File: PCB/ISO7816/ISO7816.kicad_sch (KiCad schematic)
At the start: 48 parts, among them J1 Conn_01x02, J3 Conn_01x08, J4 Conn_01x08, J6 USB-C-Socket-H, J7 TC2030-USB-NL-DS, Q1 BSS138PS, Q2 BSS138PS, Q3 BSS138PS, U1 ESP32-S3-MINI-1-N4R2, U2 TPS562246, U4 TPS22916CNYFPR, U5 TPS22916CNYFPR

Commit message: Schematic
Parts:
- removed C1, C9: C, RevK:C_0805, symbol Device:C
- removed C10, C11, C12, C13, C14, C7, C8: C, RevK:C_0201, symbol Device:C
- removed C2, C3, C4: C, RevK:C_0402, symbol Device:C
- removed C5: C, RevK:C_0603, symbol Device:C
- removed D4: ~, RevK:DFN1006-2L, symbol RevK:ES05D1MC10
- removed L1: L, RevK:L_5x5, symbol Device:L
- removed unit 1 of Q2
- removed R7: R, RevK:R_0201, symbol Device:R
- removed U2: TPS562246, RevK:SOT-563, symbol RevK:TPS562246
- added C15: 22uF 25V, RevK:C_0805, symbol Device:C
- added C16, C17: 100nF 25V, RevK:C_0402, symbol Device:C
- added C18, C21, C22, C23, C24, C25: 100nF, RevK:C_0201, symbol Device:C
- added C19: 18pF, RevK:C_0201, symbol Device:C
- added C20: 47uF 6V, RevK:C_0805, symbol Device:C
- added L2: 4.7uH, RevK:L_5x5, symbol Device:L
- added Q3: BSS138PS, RevK:SOT-363_SC-70-6, symbol RevK:BSS138PS
- added Q4: BSS84, Package_TO_SOT_SMD:SOT-23, symbol Transistor_FET:BSS84
- added R14, R15: 150k 1%, RevK:R_0201, symbol Device:R
- added R16: 33k 1%, RevK:R_0201, symbol Device:R
- added R17, R18, R19: 10k, RevK:R_0201, symbol Device:R
- added R20: 10R, RevK:R_0201, symbol Device:R
- added U2, U6: SN74LVC1T45DCK, Package_TO_SOT_SMD:SOT-363_SC-70-6, symbol Logic_LevelTranslator:SN74LVC1T45DCK
- added U3: TPS562246, RevK:SOT-563, symbol RevK:TPS562246
- C6: value C -> 1uF; footprint RevK:C_0402 -> RevK:C_0201
- J3, J4: now left out of the parts list
- R1: value R -> 20k; MPN C310173 -> (none)
- R2: value R -> 10k; footprint RevK:R_0402 -> RevK:R_0201
- R3: value R -> 10k; MPN C310173 -> (none)
- R4: value R -> 10k; MPN C320835 -> (none)
- renumbered Q3 to Q2
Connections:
- net +3.3V: now also C19.2, C20.1, C21.2, C22.2, C23.2, C24.2, C25.2, L2.2, R15.1, U2.1 (VCCA), U6.1 (VCCA); no longer R3.1
- net BST: now also C18.1, U3.4 (VBST)
- net C_3V3: now also U1.41 (GPIO45)
- net C_5V: now also U1.38 (GPIO42)
- net C_INSERT: now also U1.22 (GPIO18)
- net C_I/O: now also R1.2, Q3.3 (SP)
- net C_I/O_I: now also U1.28 (GPIO33)
- net C_RST: now also R20.2
- net C_VCC: now also R3.2, Q4.2 (S), U2.6 (VCCB), U6.6 (VCCB)
- net C_VCC_I: now also U1.36 (GPIO40)
- net C_VPP_I: now also U1.37 (GPIO41)
- net EN: now also R14.1, U3.5 (EN); no longer R1.1
- net FB: now also C19.1, R15.2, R16.1, U3.6 (VFB); no longer R3.2, R4.1
- net GND: now also R4.1, C15.2, C16.2, C17.2, C20.2, C21.1, C22.1, C23.1, C24.1, C25.1, Q3.1 (SN), Q3.4 (DP), R16.2, R17.2, R18.1, R19.1, U2.2 (GND), U3.3 (GND), U6.2 (GND); no longer Q2.4 (DP), R4.2
- net LED: now also U1.5 (GPIO1); no longer U1.27 (GPIO47)
- net SW: now also C18.2, L2.1, U3.2 (SW)
- net VBUS: now also C15.1, C16.1, C17.1, R14.2, U3.1 (VIN); no longer R1.2
- net at Q1.5 (GP), R6.1: no longer D3.2
- net at D5.2, R8.1: now also U6.4 (B); no longer Q2.5 (GP)
- net C_RST_E: now reaches U1.33 (GPIO37)
- net C_RST_E: now also R19.2, U2.5 (DIR)
- net C_CLK_IO: now reaches U1.34 (GPIO38)
- net C_CLK_IO: now also U6.3 (A)
- net C_CLK_E: now reaches U1.35 (GPIO39)
- net C_CLK_E: now also R18.2, U6.5 (DIR)
- net C_CLK_I: no longer names the net of Q2.3 (SP)
- net RX renamed C_I/O_E
- net C_I/O_E: now also R4.2, Q3.2 (GN)
- net RX2 renamed C_I/O_O
- net C_I/O_O: now also Q3.5 (GP), R17.1
- net TX: no longer names the net of U1.30 (GPIO48)
- net TX2 renamed C_RST_IO
- net C_RST_IO: now also U2.3 (A)
- new net: D3.2, R20.1, U2.4 (B)
- new net: Q4.3 (D), R1.1
- new net: Q3.6 (DN), Q4.1 (G), R3.1
- no-connect marks 31 -> 26
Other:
- note removed: "TODO CARD DRIVING"
- moved on the sheet: C6, D2, D5, D6, Q1A, Q1B, Q2A, R2, R5, R6, R8, R9

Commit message: Ready to order
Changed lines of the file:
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@@
 	)
 	(global_label "C_VPP"
-		(shape input)
+		(shape bidirectional)
 		(at 226.695 79.375 180)
 		(fields_autoplaced yes)
@@
 		)
 		(property "Intersheetrefs" "${INTERSHEET_REFS}"
-			(at 218.4978 79.375 0)
+			(at 217.5453 79.375 0)
 			(effects
 				(font
@@
 	)
 	(global_label "C_VCC"
-		(shape input)
+		(shape bidirectional)
 		(at 226.695 66.675 180)
 		(fields_autoplaced yes)
@@
 		)
 		(property "Intersheetrefs" "${INTERSHEET_REFS}"
-			(at 218.4978 66.675 0)
+			(at 217.5453 66.675 0)
 			(effects
 				(font
@@
 	)
 	(global_label "C_RST"
-		(shape input)
+		(shape bidirectional)
 		(at 226.695 69.215 180)
 		(fields_autoplaced yes)
@@
 		)
 		(property "Intersheetrefs" "${INTERSHEET_REFS}"
-			(at 218.6793 69.215 0)
+			(at 217.7268 69.215 0)
 			(effects
 				(font
@@
 	)
 	(global_label "C_VCC"
-		(shape input)
+		(shape bidirectional)
 		(at 226.695 43.18 180)
 		(fields_autoplaced yes)
@@
 		)
 		(property "Intersheetrefs" "${INTERSHEET_REFS}"
-			(at 218.4978 43.18 0)
+			(at 217.5453 43.18 0)
 			(effects
 				(font
@@
 	)
 	(global_label "C_CLK"
-		(shape input)
+		(shape bidirectional)
 		(at 226.695 71.755 180)
 		(fields_autoplaced yes)
@@
 		)
 		(property "Intersheetrefs" "${INTERSHEET_REFS}"
-			(at 218.5583 71.755 0)
+			(at 217.6058 71.755 0)
 			(effects
 				(font
@@
 	)
 	(global_label "C_RST"
-		(shape input)
+		(shape bidirectional)
 		(at 226.695 45.72 180)
 		(fields_autoplaced yes)
@@
 		)
 		(property "Intersheetrefs" "${INTERSHEET_REFS}"
-			(at 218.6793 45.72 0)
+			(at 217.7268 45.72 0)
 			(effects
 				(font
@@
 	)
 	(global_label "C_VPP"
-		(shape input)
+		(shape bidirectional)
 		(at 226.695 55.88 180)
 		(fields_autoplaced yes)
@@
 		)
 		(property "Intersheetrefs" "${INTERSHEET_REFS}"
-			(at 218.4978 55.88 0)
-			(effects
-				(font
+			(at 217.5453 55.88 0)
+			(effects
+				(font

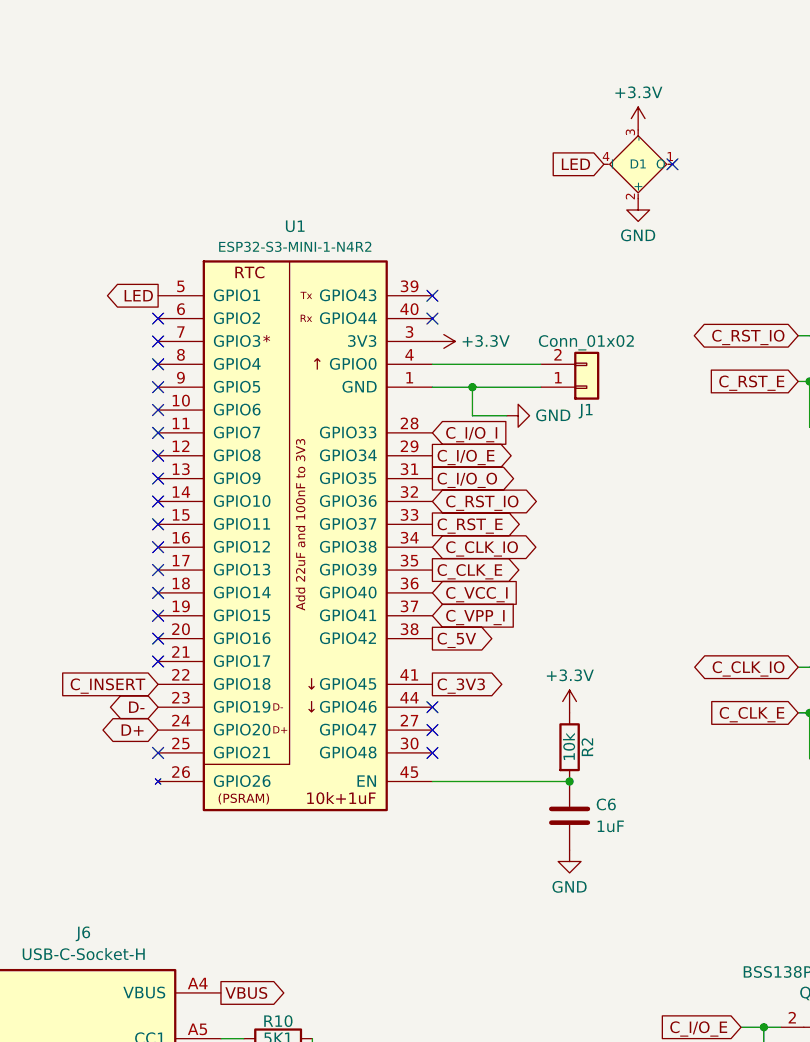
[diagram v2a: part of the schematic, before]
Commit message: Added serial
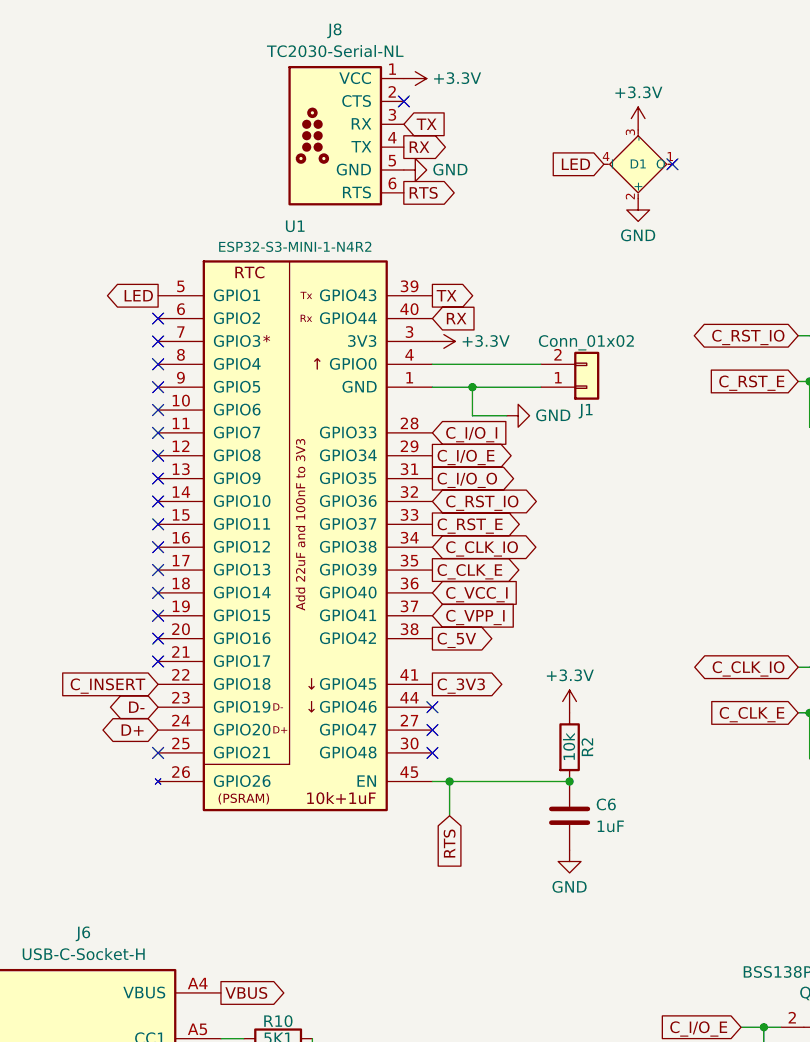
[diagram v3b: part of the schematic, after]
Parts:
- added J8: TC2030-Serial-NL, RevK:Tag-Connect_TC2030-IDC-NL_2x03_P1.27mm_Vertical, symbol RevK:TC2030-Serial-NL
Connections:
- net +3.3V: now also J8.1 (VCC)
- net GND: now also J8.5 (GND)
- net RTS: now reaches C6.1, R2.2, U1.45 (EN)
- net RTS: now also J8.6 (RTS)
- net TX: now reaches U1.39 (GPIO43)
- net TX: now also J8.3 (RX)
- net RX: now reaches U1.40 (GPIO44)
- net RX: now also J8.4 (TX)
- no-connect marks 26 -> 25
